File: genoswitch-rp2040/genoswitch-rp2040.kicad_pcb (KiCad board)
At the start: 2 copper layers, 43.4 x 49 mm, 44 parts, among them J1 USB_B_Micro, J10 RP2040_ADC2, J11 RP2040_ADC3, J2 Conn_01x03_Socket-PicoDebug, J3 HW-SPI0, J4 HW-SPI1, J5 PIO-SPI0, J6 PIO-SPI1, J7 SERIAL, J8 RP2040_ADC0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

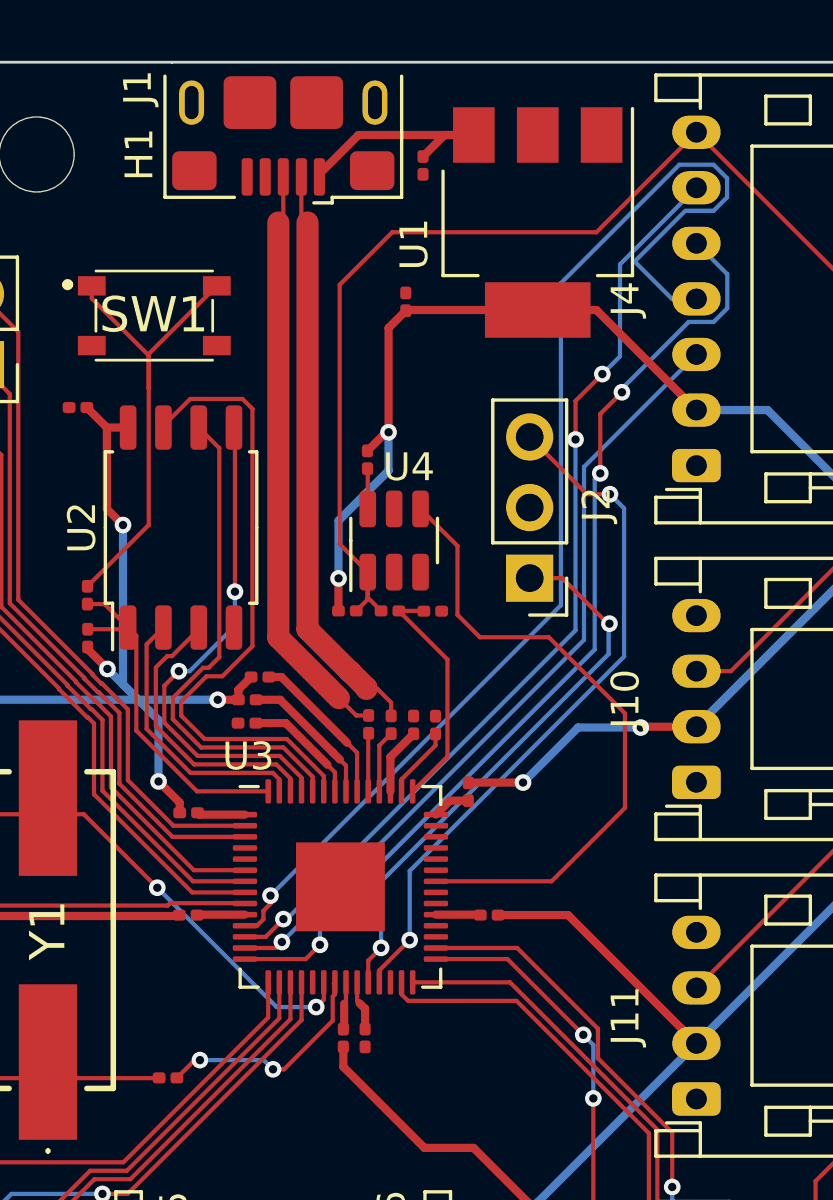
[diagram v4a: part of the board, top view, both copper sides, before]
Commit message: Route 1v1 rail, 3v3 links between U1 outputs
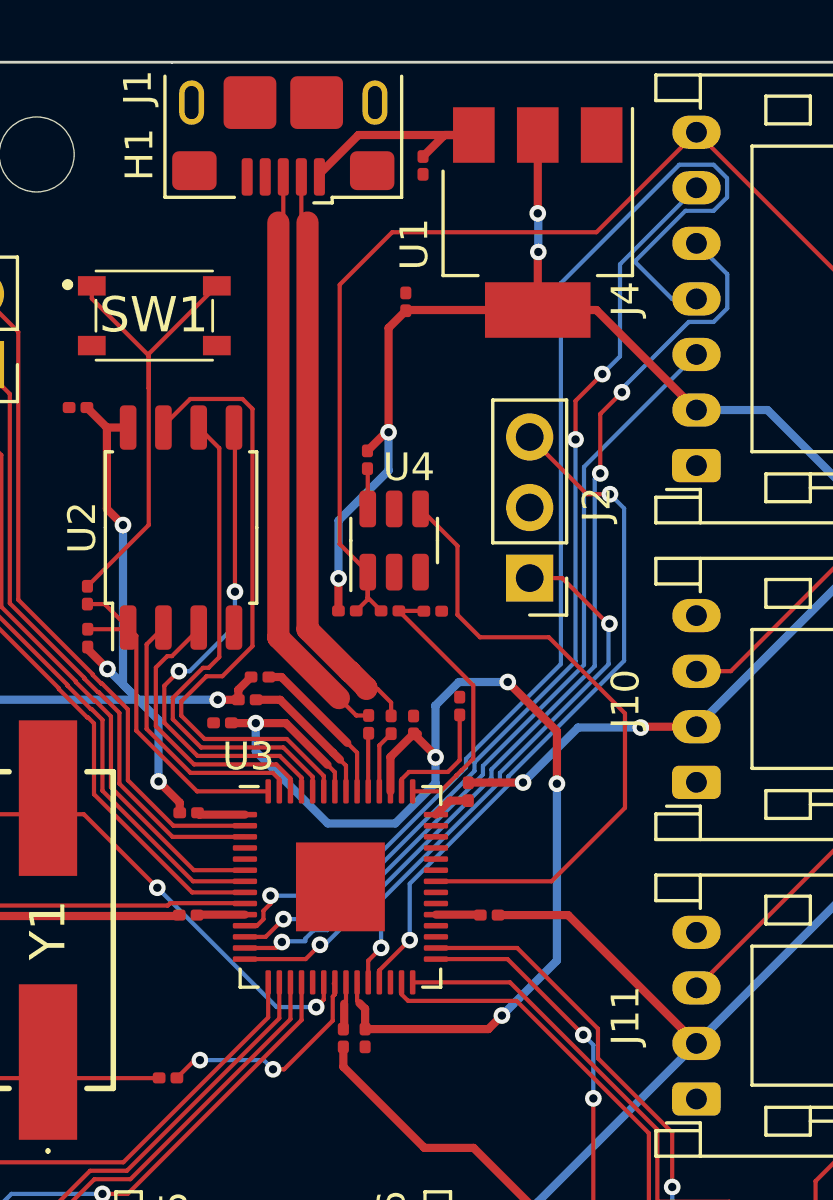
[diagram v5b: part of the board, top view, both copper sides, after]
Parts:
- moved C10 1.11 mm to (113.6, 67.4)
- moved C6 0.88 mm to (105.1, 68.0)
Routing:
- net +1V1: track 8.49 -> 44.3 mm, vias 0 -> 5
- net +3V3: track 269.7 -> 276.1 mm, vias 8 -> 10
- net Net-(U3-VREG_IN): track 2.57 -> 4.44 mm
- net /GPIO8: track 43.8 -> 45.2 mm
- net /ADC_AVDD: track 8.64 -> 10.0 mm
- net /GPIO9: track 34.2 -> 35.0 mm
- net /GPIO10: track 28.8 -> 29.5 mm

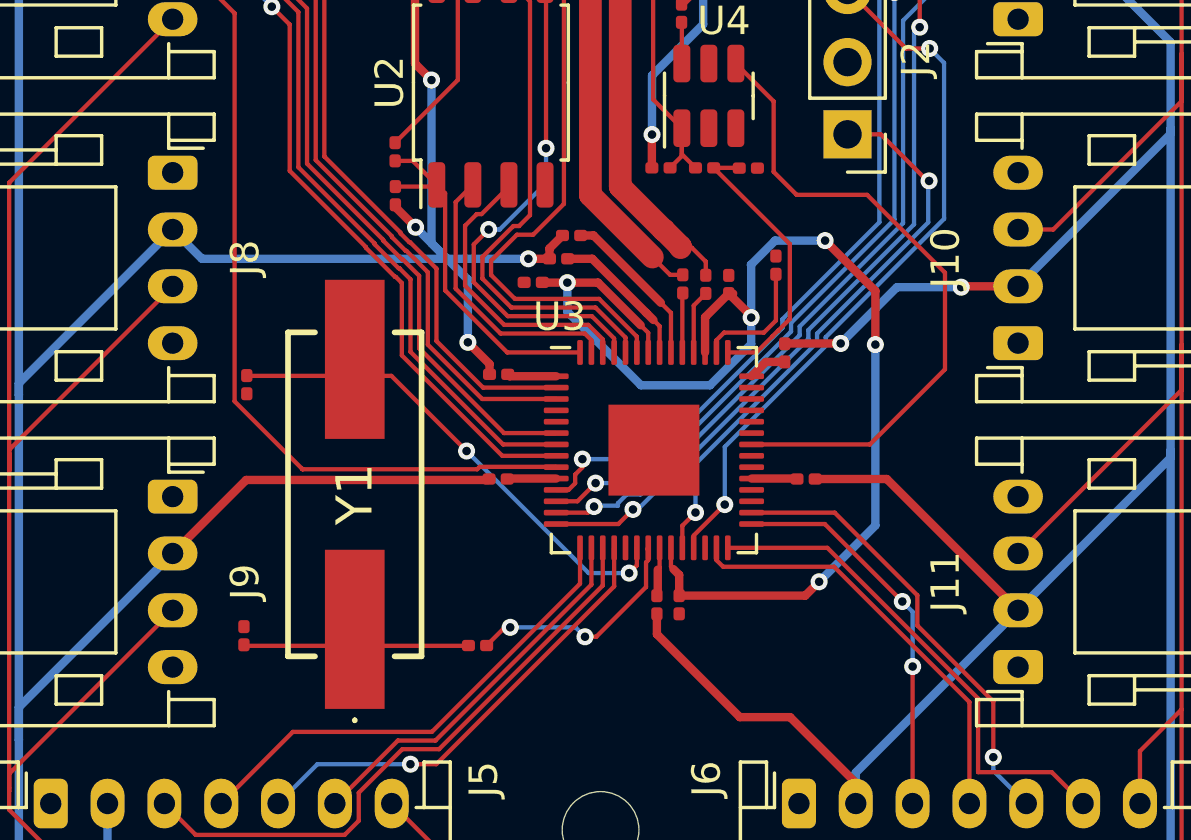
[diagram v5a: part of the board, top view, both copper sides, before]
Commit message: Route ADC pins to headers
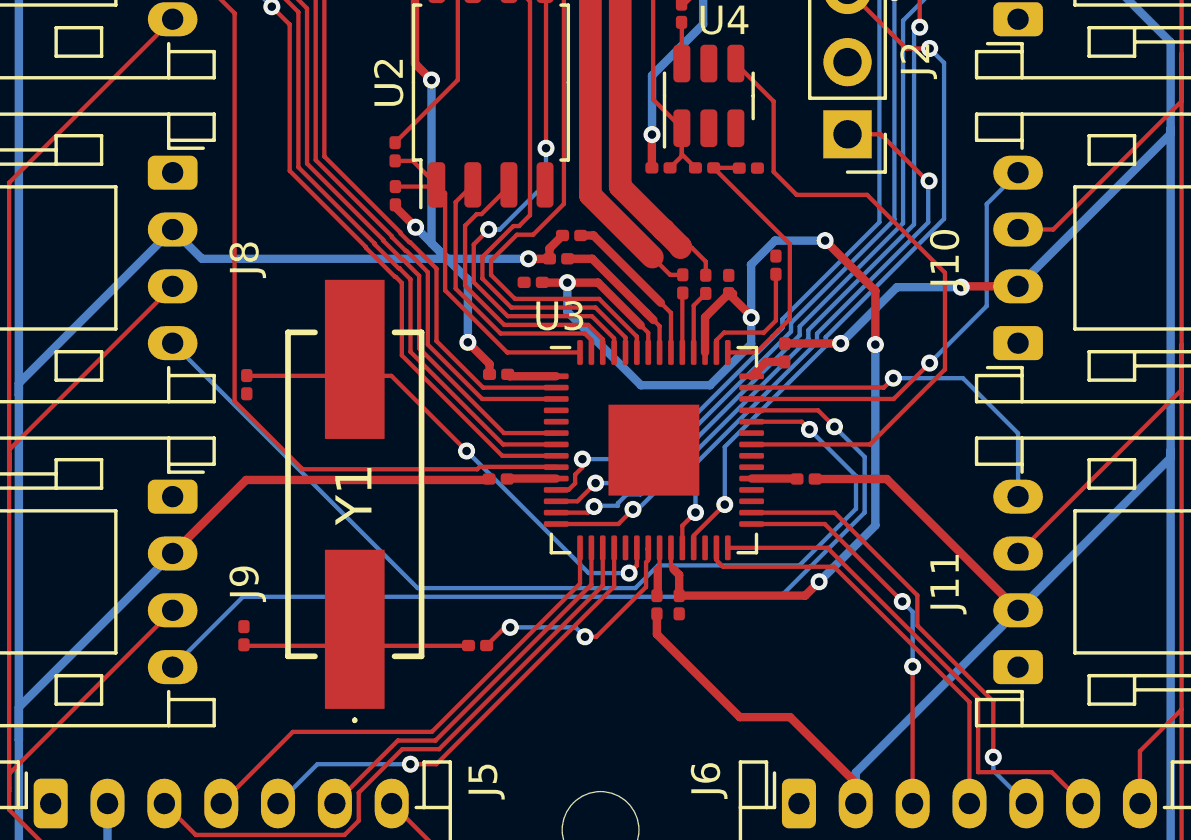
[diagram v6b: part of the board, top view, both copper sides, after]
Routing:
- net /GPIO26_ADC0: track 0.00 -> 34.4 mm, vias 0 -> 1
- net /GPIO27_ADC1: track 0.00 -> 33.2 mm, vias 0 -> 1
- net /GPIO28_ADC2: track 0.00 -> 14.8 mm, vias 0 -> 1
- net /GPIO29_ADC3: track 0.00 -> 12.5 mm, vias 0 -> 1
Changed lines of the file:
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@@
   (segment (start 119.59 67.67) (end 119.59 71.07) (width 0.1524) (layer "F.Cu") (net 49))
   (segment (start 113.56 64.12) (end 114.37 64.93) (width 0.1524) (layer "F.Cu") (net 49))
+  (segment (start 114.82 73.1859) (end 114.5481 72.914) (width 0.1524) (layer "F.Cu") (net 51))
+  (segment (start 114.5481 72.914) (end 112.7845 72.914) (width 0.1524) (layer "F.Cu") (net 51))
+  (via (at 114.82 73.1859) (size 0.6) (drill 0.3) (layers "F.Cu" "B.Cu") (net 51))
+  (segment (start 116.458772 74.824672) (end 116.458772 75.980176) (width 0.1524) (layer "B.Cu") (net 51))
+  (segment (start 114.468948 77.97) (end 109.493554 77.97) (width 0.1524) (layer "B.Cu") (net 51))
+  (segment (start 116.458772 75.980176) (end 114.468948 77.97) (width 0.1524) (layer "B.Cu") (net 51))
+  (segment (start 101.0315 78.7695) (end 92.412 70.15) (width 0.1524) (layer "B.Cu") (net 51))
+  (segment (start 109.493554 77.97) (end 108.694054 78.7695) (width 0.1524) (layer "B.Cu") (net 51))
+  (segment (start 108.694054 78.7695) (end 101.0315 78.7695) (width 0.1524) (layer "B.Cu") (net 51))
+  (segment (start 114.82 73.1859) (end 116.458772 74.824672) (width 0.1524) (layer "B.Cu") (net 51))
+  (segment (start 112.7845 72.514) (end 115.124 72.514) (width 0.1524) (layer "F.Cu") (net 52))
+  (segment (start 115.124 72.514) (end 115.7 73.09) (width 0.1524) (layer "F.Cu") (net 52))
+  (via (at 115.7 73.09) (size 0.6) (drill 0.3) (layers "F.Cu" "B.Cu") (net 52))
+  (segment (start 116.763572 74.153572) (end 116.763572 76.106428) (width 0.1524) (layer "B.Cu") (net 52))
+  (segment (start 116.763572 76.106428) (end 113.7957 79.0743) (width 0.1524) (layer "B.Cu") (net 52))
+  (segment (start 115.7 73.09) (end 116.763572 74.153572) (width 0.1524) (layer "B.Cu") (net 52))
+  (segment (start 94.8877 79.0743) (end 92.412 81.55) (width 0.1524) (layer "B.Cu") (net 52))
+  (segment (start 113.7957 79.0743) (end 94.8877 79.0743) (width 0.1524) (layer "B.Cu") (net 52))
+  (segment (start 112.7845 72.114) (end 117.786 72.114) (width 0.1524) (layer "F.Cu") (net 53))
+  (segment (start 117.786 72.114) (end 119.05 70.85) (width 0.1524) (layer "F.Cu") (net 53))
+  (via (at 119.05 70.85) (size 0.6) (drill 0.3) (layers "F.Cu" "B.Cu") (net 53))
+  (segment (start 119.05 70.85) (end 121.0584 68.8416) (width 0.1524) (layer "B.Cu") (net 53))
+  (segment (start 121.0584 68.8416) (end 121.0584 65.2536) (width 0.1524) (layer "B.Cu") (net 53))
+  (segment (start 121.0584 65.2536) (end 122.162 64.15) (width 0.1524) (layer "B.Cu") (net 53))
+  (segment (start 117.439152 71.714) (end 117.771576 71.381576) (width 0.1524) (layer "F.Cu") (net 54))
+  (segment (start 112.7845 71.714) (end 117.439152 71.714) (width 0.1524) (layer "F.Cu") (net 54))
+  (via (at 117.771576 71.381576) (size 0.6) (drill 0.3) (layers "F.Cu" "B.Cu") (net 54))
+  (segment (start 117.771576 71.381576) (end 120.221576 71.381576) (width 0.1524) (layer "B.Cu") (net 54))
+  (segment (start 120.221576 71.381576) (end 122.162 73.322) (width 0.1524) (layer "B.Cu") (net 54))
+  (segment (start 122.162 73.322) (end 122.162 75.55) (width 0.1524) (layer "B.Cu") (net 54))
   (segment (start 110.347 70.4765) (end 110.347 68.4) (width 0.1524) (layer "F.Cu") (net 55))
   (segment (start 110.347 68.4) (end 110.362 68.385) (width 0.1524) (layer "F.Cu") (net 55))

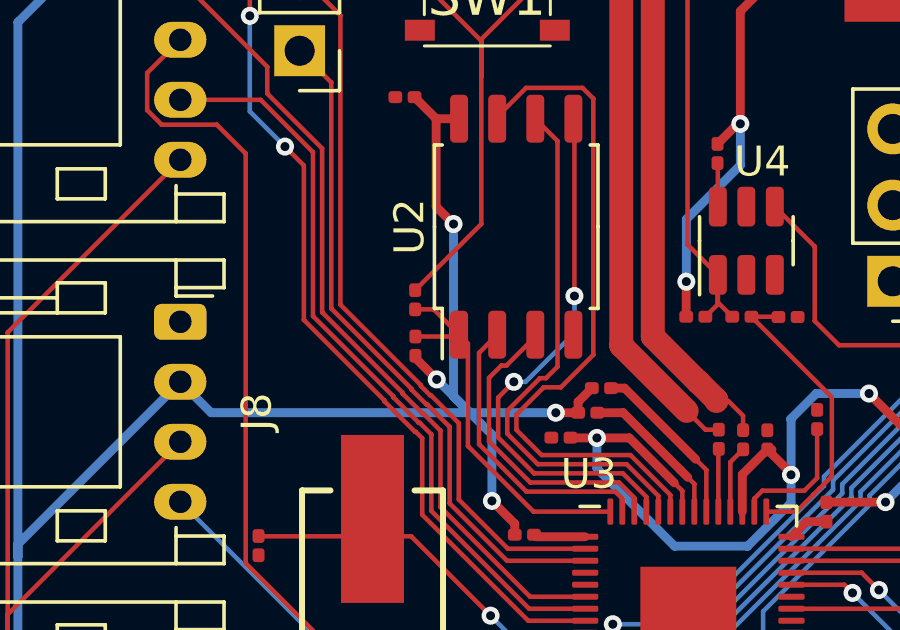
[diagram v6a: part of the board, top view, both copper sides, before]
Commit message: Adjust positioning of +3v3 rail near U2
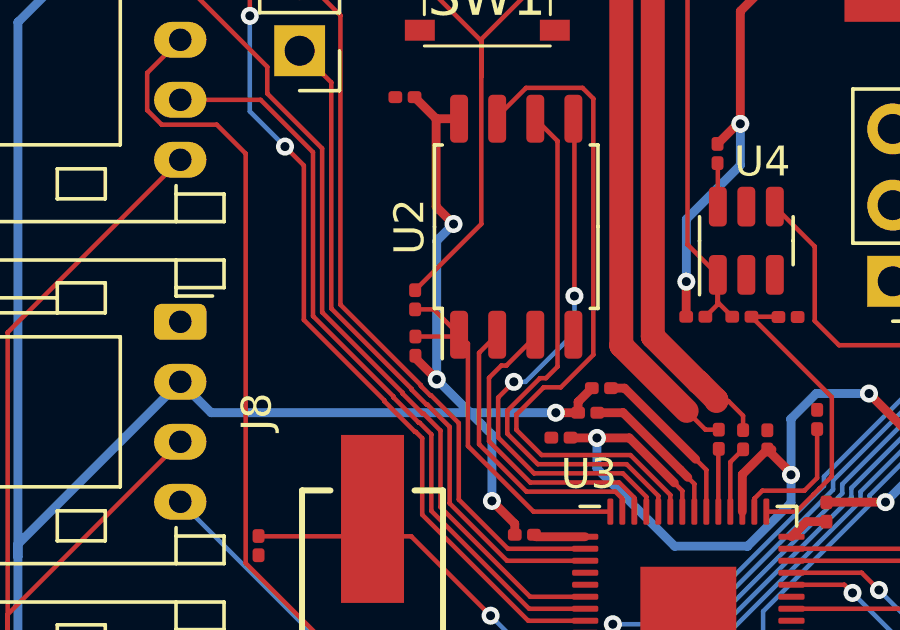
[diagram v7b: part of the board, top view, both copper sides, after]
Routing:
- net +3V3: track 276.1 -> 275.3 mm
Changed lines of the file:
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@@
   (segment (start 127.53 91.34) (end 126.817828 92.052172) (width 0.295656) (layer "B.Cu") (net 5))
   (segment (start 90.862172 92.052172) (end 90.705 91.895) (width 0.295656) (layer "B.Cu") (net 5))
-  (segment (start 101.52 66.63) (end 101.845 66.955) (width 0.295656) (layer "B.Cu") (net 5))
   (segment (start 101.845 66.955) (end 102.07 67.18) (width 0.295656) (layer "B.Cu") (net 5))
   (segment (start 126.817828 92.052172) (end 90.862172 92.052172) (width 0.295656) (layer "B.Cu") (net 5))
@@
   (segment (start 93.442 67.18) (end 92.412 66.15) (width 0.295656) (layer "B.Cu") (net 5))
   (segment (start 127.53 62.61) (end 127.53 62.782) (width 0.295656) (layer "B.Cu") (net 5))
+  (segment (start 101.52 60.89) (end 100.96 61.45) (width 0.295656) (layer "B.Cu") (net 5))
   (segment (start 87 82.962) (end 92.412 77.55) (width 0.295656) (layer "B.Cu") (net 5))
   (segment (start 104.93 67.18) (end 102.07 67.18) (width 0.295656) (layer "B.Cu") (net 5))
@@
   (segment (start 87 71.562) (end 92.412 66.15) (width 0.295656) (layer "B.Cu") (net 5))
   (segment (start 116.47 49.69) (end 116.45 49.67) (width 0.295656) (layer "B.Cu") (net 5))
+  (segment (start 100.96 61.45) (end 100.96 66.07) (width 0.295656) (layer "B.Cu") (net 5))
   (segment (start 122.162 56.75) (end 124.72 56.75) (width 0.295656) (layer "B.Cu") (net 5))
   (segment (start 102.8 67.91) (end 101.845 66.955) (width 0.295656) (layer "B.Cu") (net 5))
@@
   (segment (start 87 88.19) (end 87 84.12) (width 0.295656) (layer "B.Cu") (net 5))
   (segment (start 111.08 58.93) (end 111.08 57.55) (width 0.295656) (layer "B.Cu") (net 5))
-  (segment (start 101.52 60.89) (end 101.52 66.63) (width 0.295656) (layer "B.Cu") (net 5))
   (segment (start 116.45 85.262) (end 122.162 79.55) (width 0.295656) (layer "B.Cu") (net 5))
   (segment (start 127.53 73.93) (end 127.53 74.182) (width 0.295656) (layer "B.Cu") (net 5))

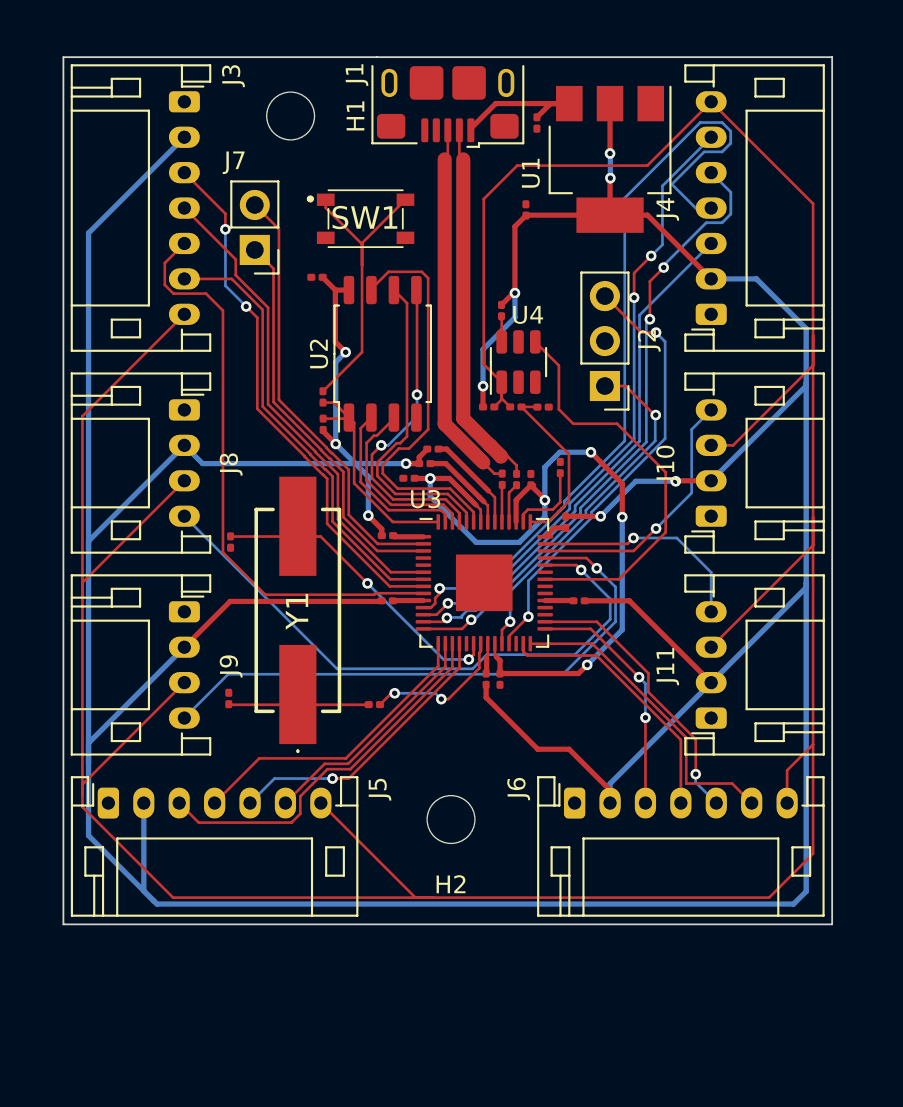
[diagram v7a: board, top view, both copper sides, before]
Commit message: Define a ground plane fill
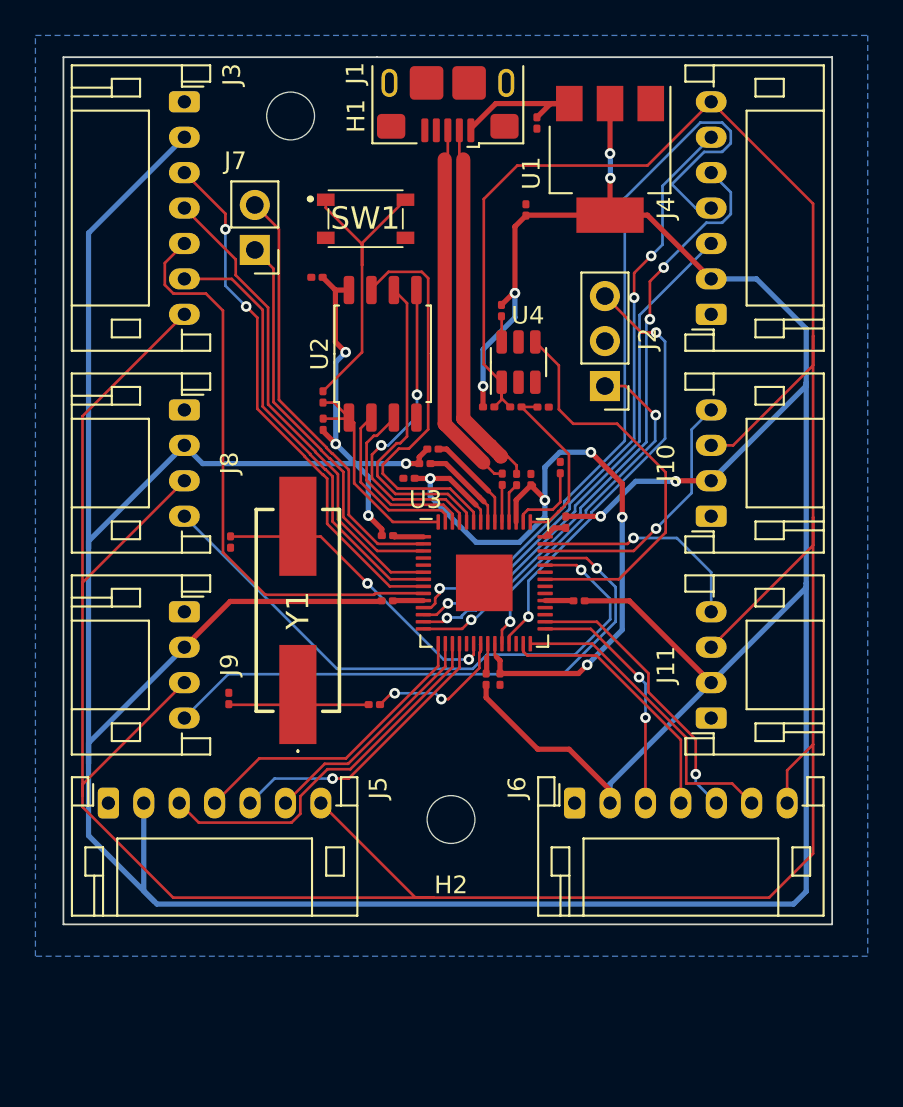
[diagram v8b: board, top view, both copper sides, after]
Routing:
- added copper zone on B.Cu, net GND
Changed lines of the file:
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@@
   (segment (start 110.747 70.4765) (end 110.747 68.825) (width 0.1524) (layer "F.Cu") (net 56))
   (segment (start 110.747 68.825) (end 111.172 68.4) (width 0.1524) (layer "F.Cu") (net 56))
+  (zone (net 2) (net_name "GND") (layer "B.Cu") (hatch edge 0.5)
+    (connect_pads (clearance 0.1524))
+    (min_thickness 0.25) (filled_areas_thickness no)
+    (fill (thermal_gap 0.5) (thermal_bridge_width 0.5))
+    (polygon
+      (pts
+        (xy 84 43)
+        (xy 131 43)
+        (xy 131 95)
+        (xy 84 95)
+      )
+    )
+  )
 )
